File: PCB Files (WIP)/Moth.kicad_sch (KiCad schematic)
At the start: 62 parts, among them J1 USB C Connector, J2 JTAG_TC2030, J3 Left Ribbon, J4 Right Ribbon, SW1 Boot, U1 XC6206, U2 USBLC6-2SC6, U3 RP2040, U4 W25Q128JVS, X1 X, Y1 12MHz, Y2 Y

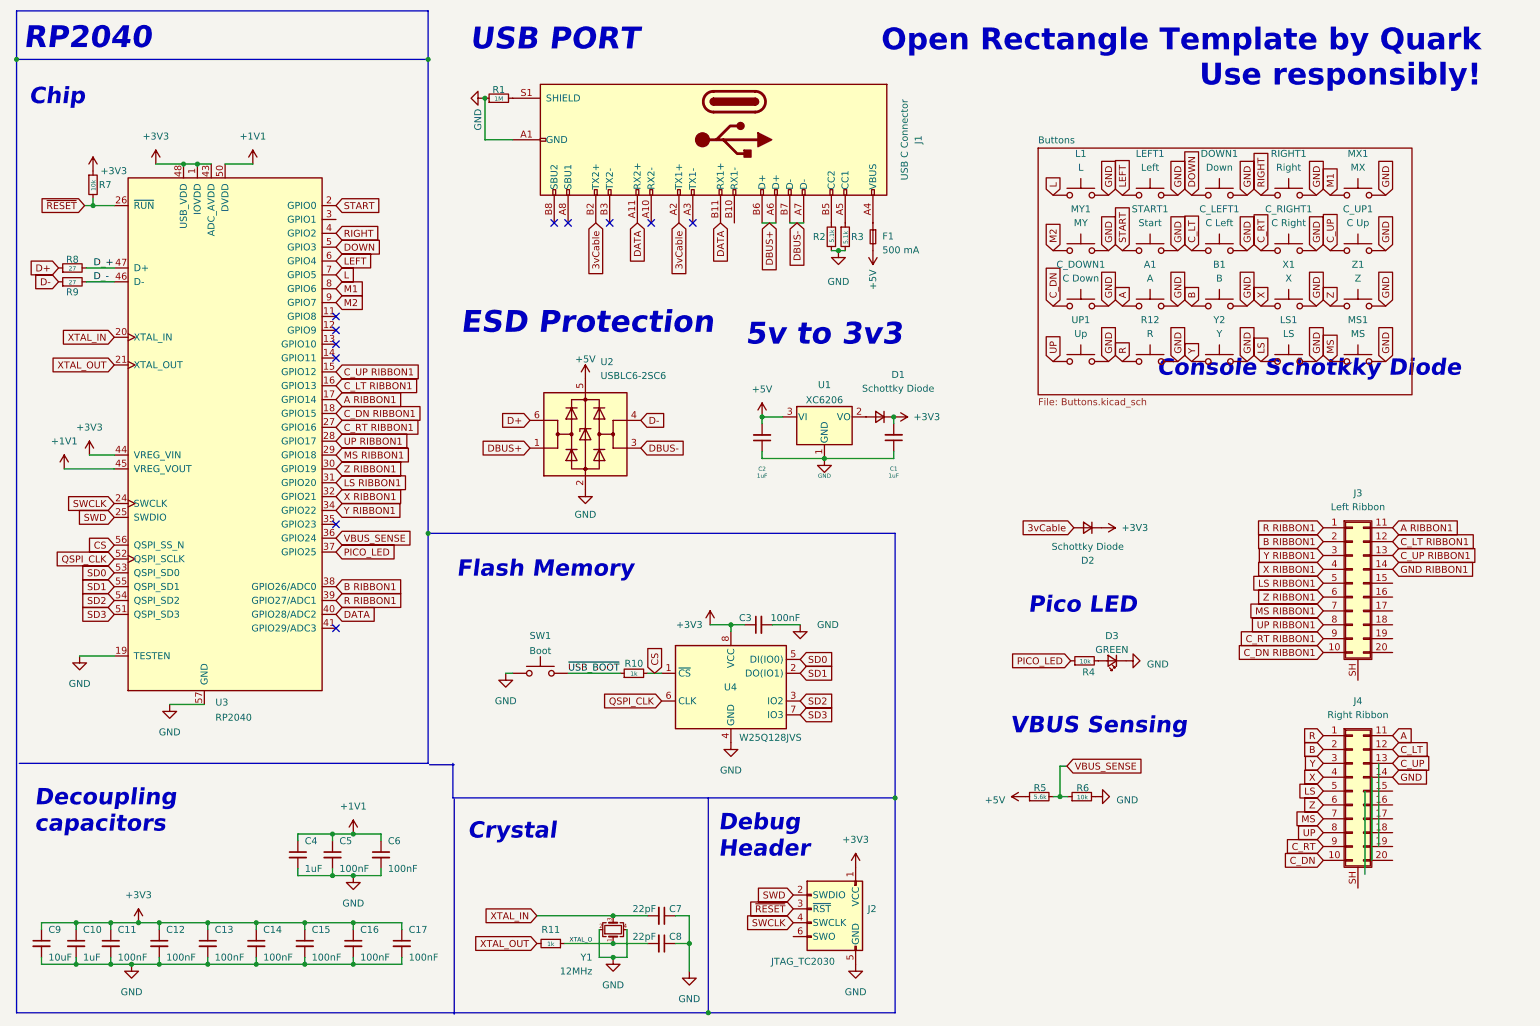
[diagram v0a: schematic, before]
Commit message: Reconfigured PCB, closer to completion.
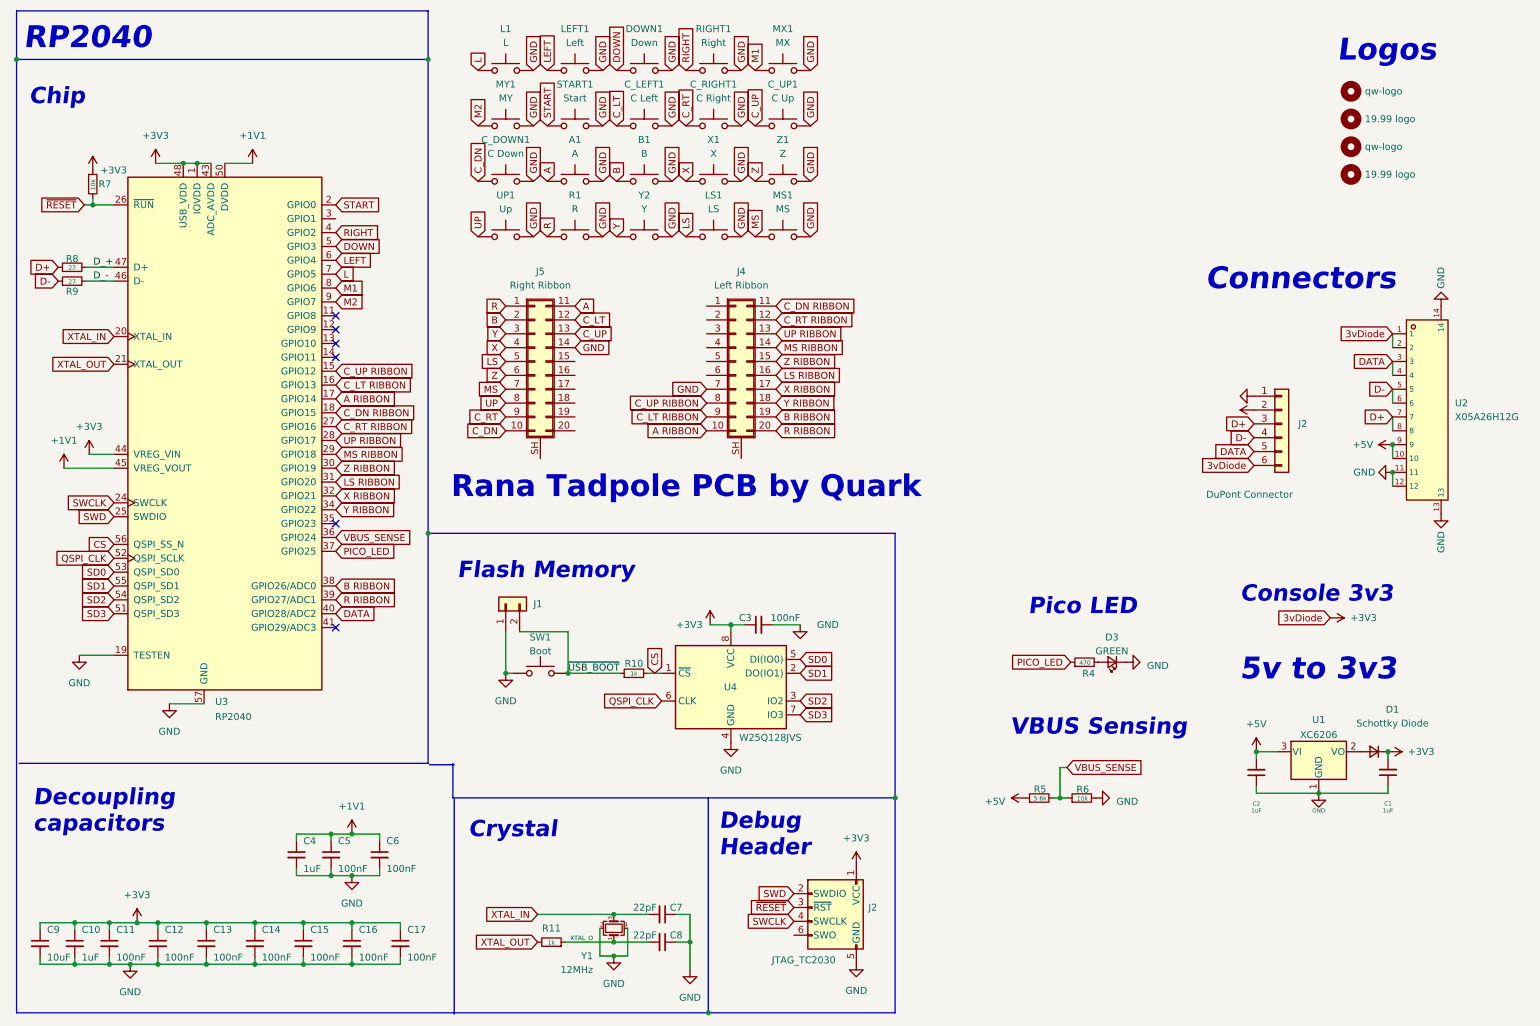
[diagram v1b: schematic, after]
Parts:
- removed D2: Schottky Diode, Diode_SMD:D_SOD-123, symbol Device:D_Small
- removed F1: 500 mA, Fuse:Fuse_1206_3216Metric, symbol Device:Fuse_Small
- removed J1: USB C Connector, footprints:TYPE-C_24P_QCHT, symbol Connector:USB_C_Receptacle
- removed J3: Left Ribbon, moth footprints:FPC-05F-30PH20, symbol Connector_Generic_Shielded:Conn_02x10_Top_Bottom_Shielded
- removed R1: 1M, Resistor_SMD:R_0603_1608Metric, symbol Device:R_Small
- removed R12: R, moth footprints:SW_Gateron_LowProfile_HotSwap_THT, symbol Switch:SW_Push
- removed R2, R3: 5.1k, Resistor_SMD:R_0402_1005Metric, symbol Device:R_Small
- removed U2: USBLC6-2SC6, Package_TO_SOT_SMD:SOT-23-6, symbol Power_Protection:USBLC6-2SC6
- added H1, H3: qw-logo, qw-logo:qw new logo silk + copper sm, symbol Mechanical:MountingHole
- added H2, H4: 19.99 logo, 1999:1999 logo md, symbol Mechanical:MountingHole
- added J1: Conn_01x02, Connector_PinHeader_2.54mm:PinHeader_1x02_P2.54mm_Vertical, symbol Connector_Generic:Conn_01x02
- added J2: DuPont Connector, Connector_PinHeader_2.54mm:PinHeader_1x06_P2.54mm_Vertical, symbol Connector_Generic:Conn_01x06
- added J5: Right Ribbon, moth footprints:FPC-05F-30PH20, symbol Connector_Generic_Shielded:Conn_02x10_Top_Bottom_Shielded
- added R1: R, moth footprints:SW_Gateron_LowProfile_HotSwap_THT, symbol Switch:SW_Push
- added U2: X05A26H12G, footprint:FPC-SMD_X05A26H12G, symbol X05A26H12G:X05A26H12G
- D3: LCSC C2297 -> C84256
- J4: value Right Ribbon -> Left Ribbon
- R4: value 10k -> 470; LCSC C25744 -> C25117
- SW1: LCSC C318884 -> C202424
- U3: footprint footprints:RP2040-QFN-56 -> qw-footprints:RP2040-QFN-56
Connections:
- net B RIBBON1 is gone; now on net B RIBBON: U3.38 (GPIO26/ADC0)
- net LS RIBBON1 is gone; now on net LS RIBBON: U3.31 (GPIO20)
- net R RIBBON1 is gone; now on net R RIBBON: U3.39 (GPIO27/ADC1)
- net X RIBBON1 is gone; now on net X RIBBON: U3.32 (GPIO21)
- net Y RIBBON1 is gone; now on net Y RIBBON: U3.34 (GPIO22)
- net Z RIBBON1 is gone; now on net Z RIBBON: U3.30 (GPIO19)
- net +3V3: now also J2.6 (Pin_6), U2.1, U2.2
- net +5V: now also J2.2 (Pin_2), U2.10, U2.9
- net A: now also J5.11 (Pin_11); no longer J4.11 (Pin_11)
- net B: now also J5.2 (Pin_2); no longer J4.2 (Pin_2)
- net C_DN: now also J5.10 (Pin_10); no longer J4.10 (Pin_10)
- net C_LT: now also J5.12 (Pin_12); no longer J4.12 (Pin_12)
- net C_RT: now also J5.9 (Pin_9); no longer J4.9 (Pin_9)
- net C_UP: now also J5.13 (Pin_13); no longer J4.13 (Pin_13)
- net D+: now also J2.3 (Pin_3), U2.7, U2.8
- net D-: now also J2.4 (Pin_4), U2.5, U2.6
- net DATA: now also J2.5 (Pin_5), U2.3, U2.4
- net GND: now also J4.7 (Pin_7), J1.1 (Pin_1), J2.1 (Pin_1), J5.14 (Pin_14), R1.2, U2.11, U2.12, U2.13, U2.14; no longer J4.14 (Pin_14)
- net LS: now also J5.5 (Pin_5); no longer J4.5 (Pin_5)
- net MS: now also J5.7 (Pin_7); no longer J4.7 (Pin_7)
- net R: now also J5.1 (Pin_1), R1.1; no longer J4.1 (Pin_1)
- net UP: now also J5.8 (Pin_8); no longer J4.8 (Pin_8)
- net X: now also J5.4 (Pin_4); no longer J4.4 (Pin_4)
- net Y: now also J5.3 (Pin_3); no longer J4.3 (Pin_3)
- net Z: now also J5.6 (Pin_6); no longer J4.6 (Pin_6)
- net ~{USB_BOOT}: now also J1.2 (Pin_2)
- net Z RIBBON: now reaches J4.15 (Pin_15)
- net LS RIBBON: now reaches J4.16 (Pin_16)
- net X RIBBON: now reaches J4.17 (Pin_17)
- net Y RIBBON: now reaches J4.18 (Pin_18)
- net B RIBBON: now reaches J4.19 (Pin_19)
- net R RIBBON: now reaches J4.20 (Pin_20)
- net A RIBBON1 renamed A RIBBON
- net A RIBBON: now also J4.10 (Pin_10)
- net C_DN RIBBON1 renamed C_DN RIBBON
- net C_DN RIBBON: now also J4.11 (Pin_11)
- net C_LT RIBBON1 renamed C_LT RIBBON
- net C_LT RIBBON: now also J4.9 (Pin_9)
- net C_RT RIBBON1 renamed C_RT RIBBON
- net C_RT RIBBON: now also J4.12 (Pin_12)
- net C_UP RIBBON1 renamed C_UP RIBBON
- net C_UP RIBBON: now also J4.8 (Pin_8)
- net MS RIBBON1 renamed MS RIBBON
- net MS RIBBON: now also J4.14 (Pin_14)
- net UP RIBBON1 renamed UP RIBBON
- net UP RIBBON: now also J4.13 (Pin_13)
- no-connect marks 11 -> 6
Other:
- removed sheet Buttons
- note added: "Connectors"
- note added: "Console 3v3"
- note added: "Logos"
- note added: "Rana Tadpole PCB by Quark"
- note removed: "Console Schotkky Diode"
- note removed: "ESD Protection"
- note removed: "Open Rectangle Template by Quark Use responsibly!"
- note removed: "USB PORT"

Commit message: Completed PCB pending review
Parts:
- removed H1, H3: qw-logo, qw-logo:qw new logo silk + copper sm, symbol Mechanical:MountingHole
- removed H2, H4: 19.99 logo, 1999:1999 logo md, symbol Mechanical:MountingHole
- A1, B1, C_DOWN1, C_LEFT1, C_RIGHT1, C_UP1, L1, LEFT1, LS1, MS1, MX1, MY1, R1, RIGHT1, START1, UP1, X1, Y2, Z1: footprint moth footprints:SW_Gateron_LowProfile_HotSwap_THT -> Box Footprints:SW_Hotswap_Kailh_Choc_V1V2_THT
- DOWN1: footprint moth footprints:SW_Gateron_LowProfile_HotSwap_THT -> Box Footprints:SW_Hotswap_Kailh_Choc_V1V2
- J4, J5: footprint moth footprints:FPC-05F-30PH20 -> Box Footprints:FPC-05F-30PH20
- U2: footprint footprint:FPC-SMD_X05A26H12G -> Box Dependecies:FPC-SMD_X05A26H12G
- U3: footprint qw-footprints:RP2040-QFN-56 -> Box Footprints:RP2040-QFN-56
